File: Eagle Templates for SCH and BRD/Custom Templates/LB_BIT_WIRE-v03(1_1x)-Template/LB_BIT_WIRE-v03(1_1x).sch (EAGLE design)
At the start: 5 parts

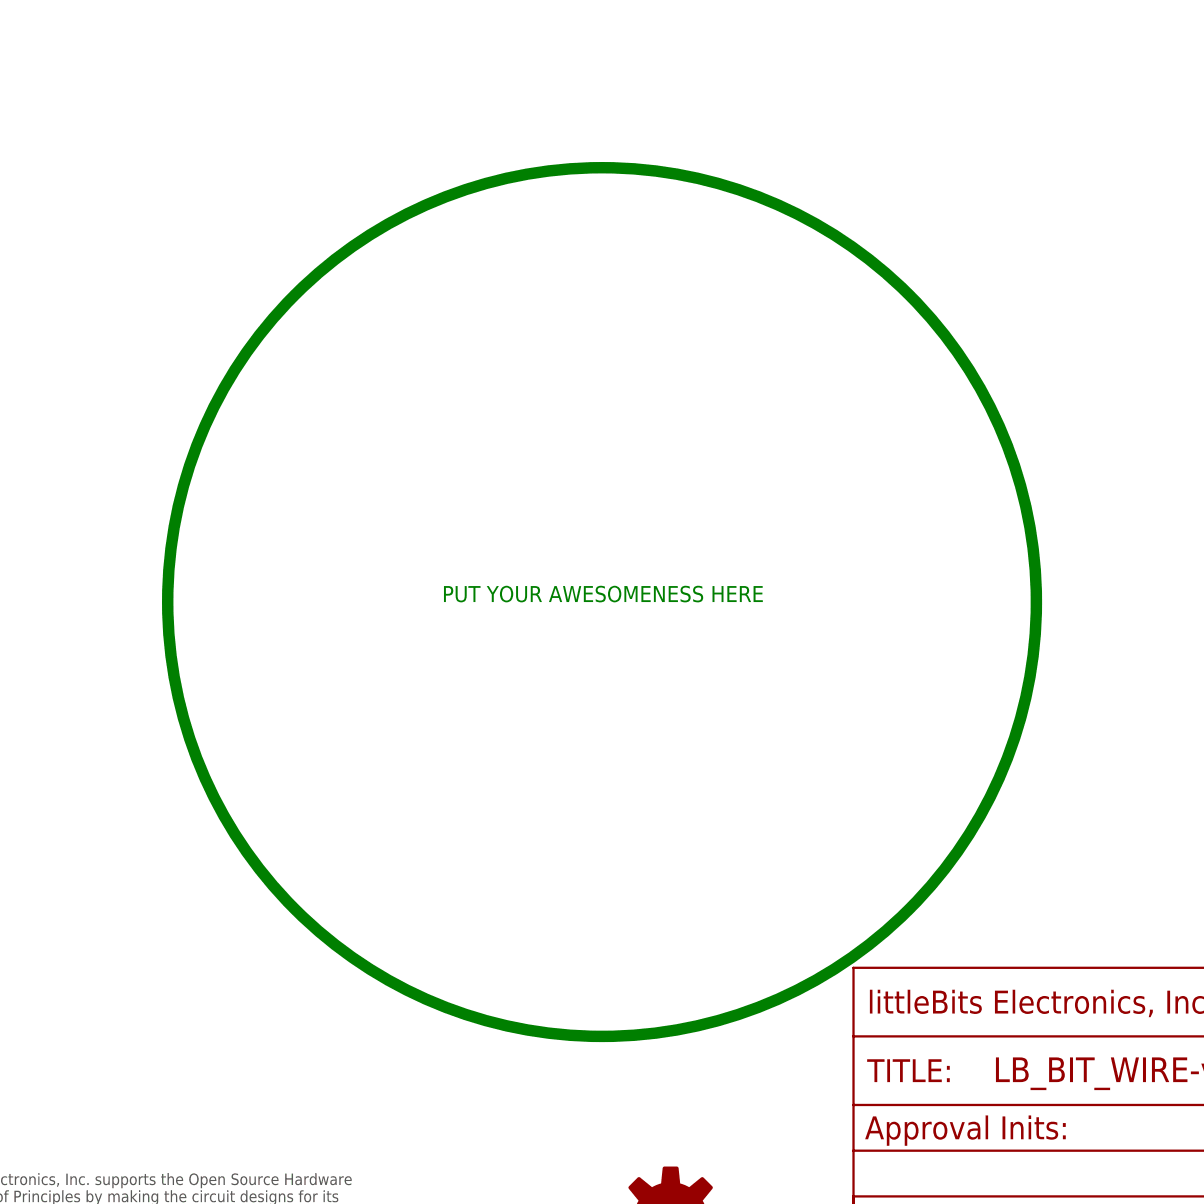
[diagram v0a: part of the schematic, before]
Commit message: Updated templates
- Added ferrite beads
- Moved text and annotations off of Nets layer
- Minor layout changes
- Removed I/O/W prefix from reference designators
- Removed output stage components from output bits
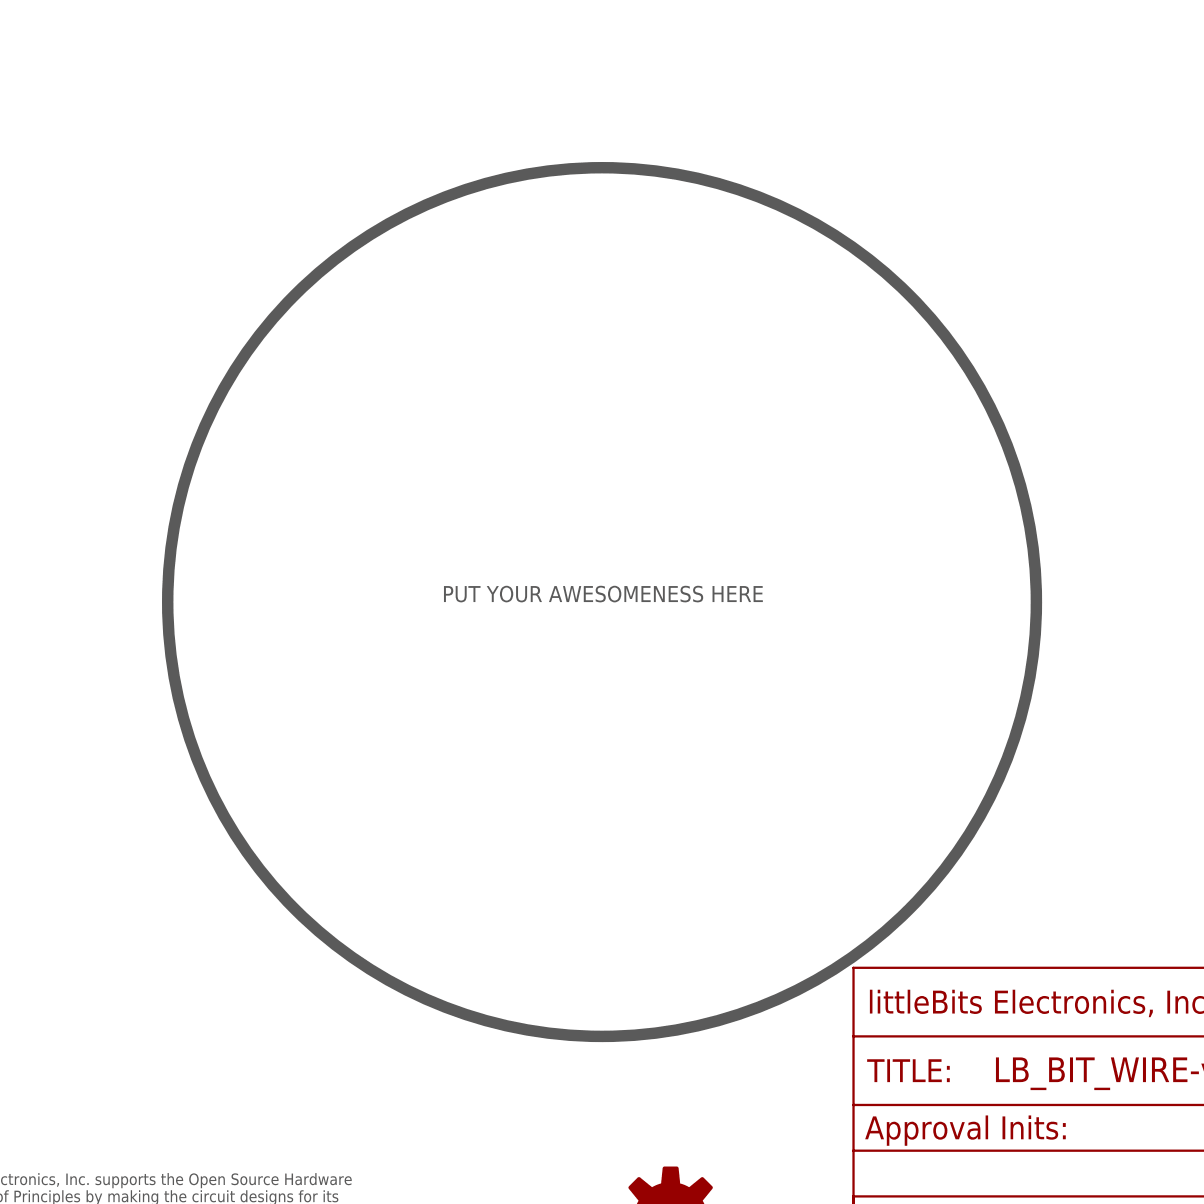
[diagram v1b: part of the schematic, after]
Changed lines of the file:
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@@
 <?xml version="1.0" encoding="utf-8"?>
 <!DOCTYPE eagle SYSTEM "eagle.dtd">
-<eagle version="6.6.0">
+<eagle version="6.5.0">
 <drawing>
 <settings>
@@
 <sheet>
 <plain>
-<circle x="119.38" y="81.28" radius="48.26" width="1.27" layer="91"/>
-<text x="101.6" y="81.28" size="1.778" layer="91">PUT YOUR AWESOMENESS HERE</text>
+<circle x="119.38" y="81.28" radius="48.26" width="1.27" layer="97"/>
+<text x="101.6" y="81.28" size="1.778" layer="97">PUT YOUR AWESOMENESS HERE</text>
 </plain>
 <instances>
